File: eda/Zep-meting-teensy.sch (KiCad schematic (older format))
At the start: 12 parts, among them P1 CONN_01X03, Q1 BC547, U1 LM358N, U2 TEMT6000_sparkfun, U3 Teensy3.2, U4 BeexyBox_B

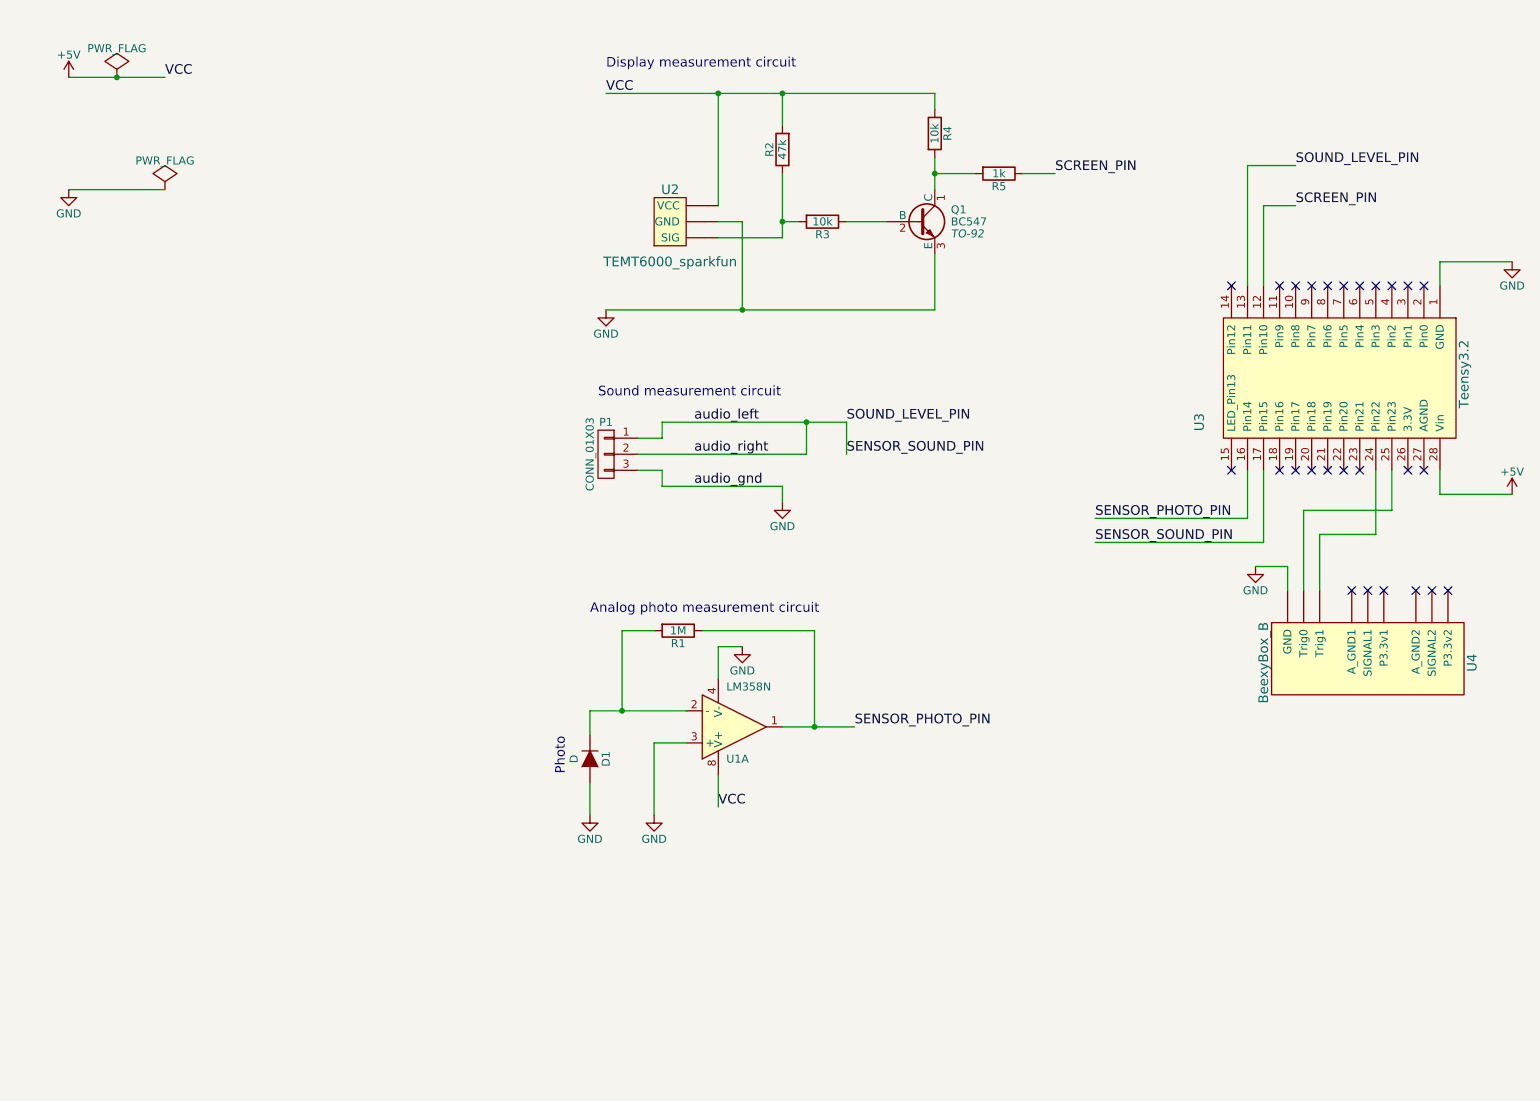
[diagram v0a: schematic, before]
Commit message: Adds opamp display sensor circuit and custom kicad eeschema parts.
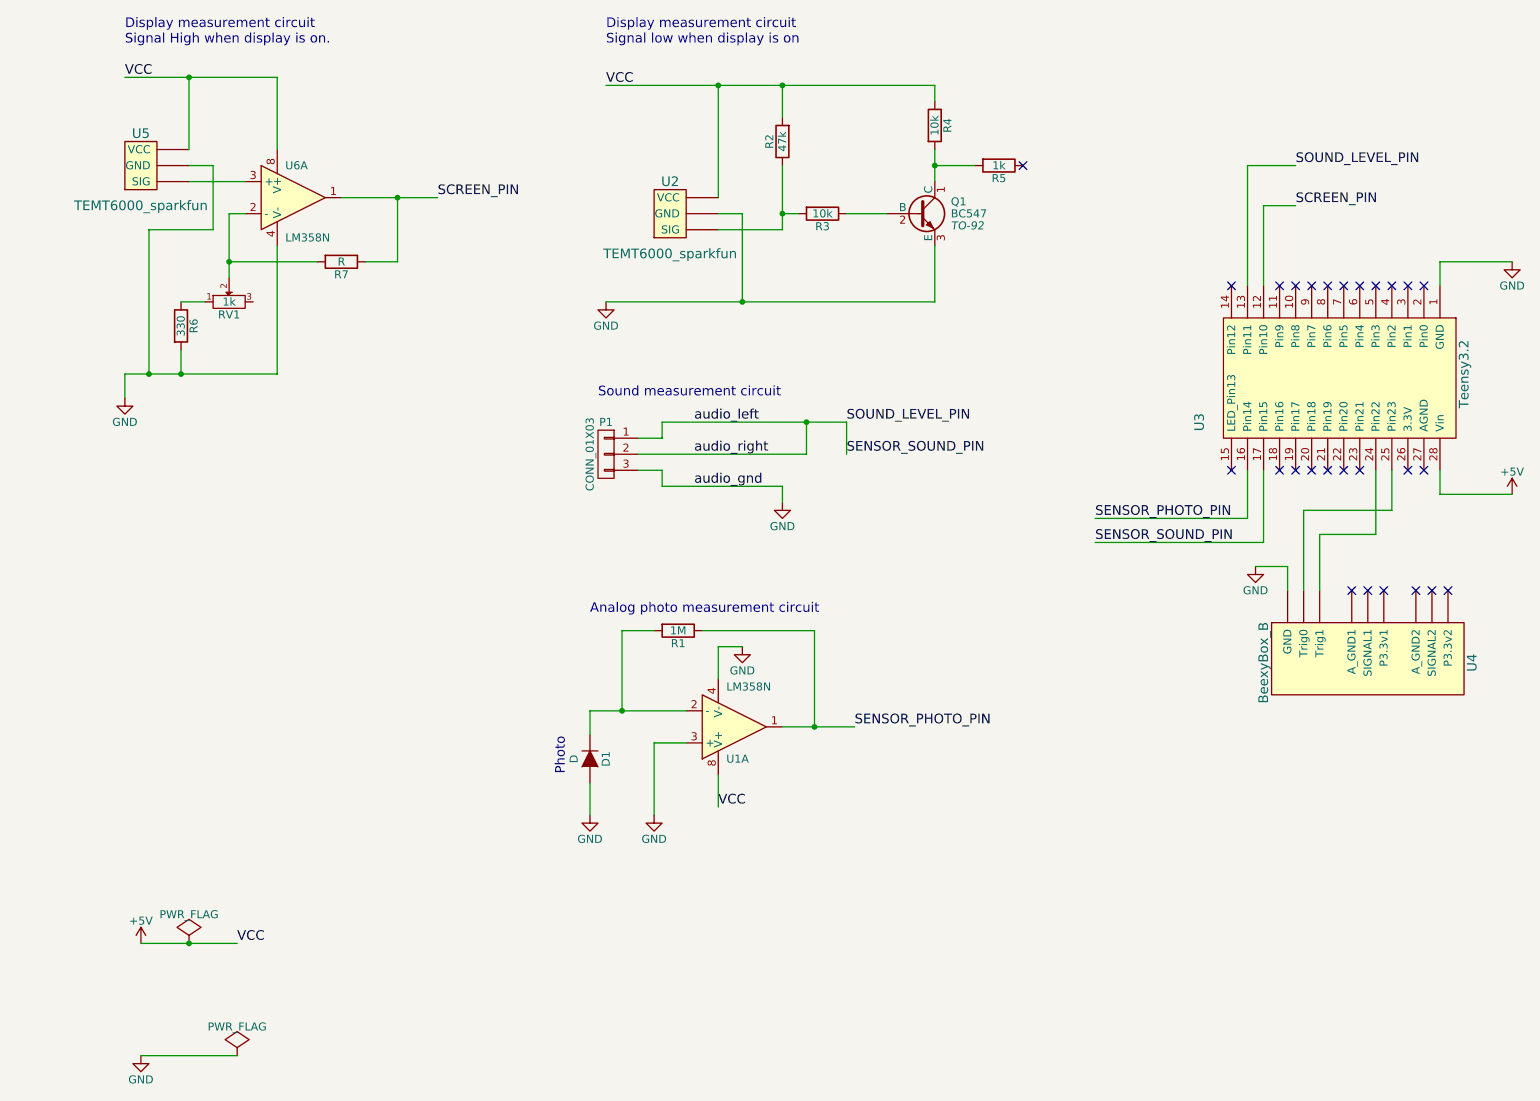
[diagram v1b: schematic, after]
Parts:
- added R6: 330, symbol R
- added R7: R, symbol R
- added RV1: 1k, symbol POT
- added U5: TEMT6000_sparkfun, symbol TEMT6000_sparkfun
- added U6: LM358N, symbol LM358N
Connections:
- net +5V: now also U5.~ (VCC), U6.8 (V+)
- net GND: now also R6.2, U5.~ (VCC), U6.4 (V-)
- net SCREEN_PIN: now also R7.1, U6.1; no longer R5.1
- new net: R6.1, RV1.1
- new net: R7.2, RV1.2, U6.2 (-)
- new net: U5.~ (VCC), U6.3 (+)
- no-connect marks 26 -> 27
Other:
- note added: "Display measurement circuit\nSignal High when display is on."
- note added: "Display measurement circuit\nSignal low when display is on"
- note removed: "Display measurement circuit\n"
- moved on the sheet: Q1, R2, R3, R4, R5, U2

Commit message: Updates electric schema
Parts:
- removed U1: LM358N, symbol LM358N
- added unit 2 of U6
- R7: value R -> 10k
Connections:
- net +5V: now also U6.4 (V-)
- net GND: now also U6.6 (-), U6.8 (V+)
- net SENSOR_PHOTO_PIN: now also U6.7
- net at D1.1 (K), R1.2: now also U6.5 (+)
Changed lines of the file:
@@
-$EndComp
-$Comp
-L LM358N U1
-U 1 1 59317688
-P 5100 5000
-F 0 "U1" H 5050 5200 50  0000 L CNN
-F 1 "LM358N" H 5050 4750 50  0000 L CNN
-F 2 "" H 5100 5000 50  0000 C CNN
-F 3 "" H 5100 5000 50  0000 C CNN
-	1    5100 5000
-	1    0    0    1
 $EndComp
 $Comp
@@
 $EndComp
 $Comp
-L LM358N U6
-U 1 1 594BCA64
-P 2350 1700
-F 0 "U6" H 2300 1900 50  0000 L CNN
-F 1 "LM358N" H 2300 1450 50  0000 L CNN
-F 2 "" H 2350 1700 50  0000 C CNN
-F 3 "" H 2350 1700 50  0000 C CNN
-	1    2350 1700
-	1    0    0    -1
-$EndComp
-$Comp
 L R R7
 U 1 1 594BCB2D
 P 2650 2100
 F 0 "R7" V 2730 2100 50  0000 C CNN
-F 1 "R" V 2650 2100 50  0000 C CNN
+F 1 "10k" V 2650 2100 50  0000 C CNN
 F 2 "" V 2580 2100 50  0000 C CNN
 F 3 "" H 2650 2100 50  0000 C CNN
@@
 Display measurement circuit\nSignal High when display is on.
 NoConn ~ 6900 1500
+$Comp
+L LM358N U6
+U 1 1 594BCA64
+P 2350 1700
+F 0 "U6" H 2300 1900 50  0000 L CNN
+F 1 "LM358N" H 2300 1450 50  0000 L CNN
+F 2 "" H 2350 1700 50  0000 C CNN
+F 3 "" H 2350 1700 50  0000 C CNN
+	1    2350 1700
+	1    0    0    -1
+$EndComp
+$Comp
+L LM358N U6
+U 2 1 594BFA45
+P 5100 5000
+F 0 "U6" H 5050 5200 50  0000 L CNN
+F 1 "LM358N" H 5050 4750 50  0000 L CNN
+F 2 "" H 5100 5000 50  0000 C CNN
+F 3 "" H 5100 5000 50  0000 C CNN
+	2    5100 5000
+	1    0    0    -1
+$EndComp
 $EndSCHEMATC

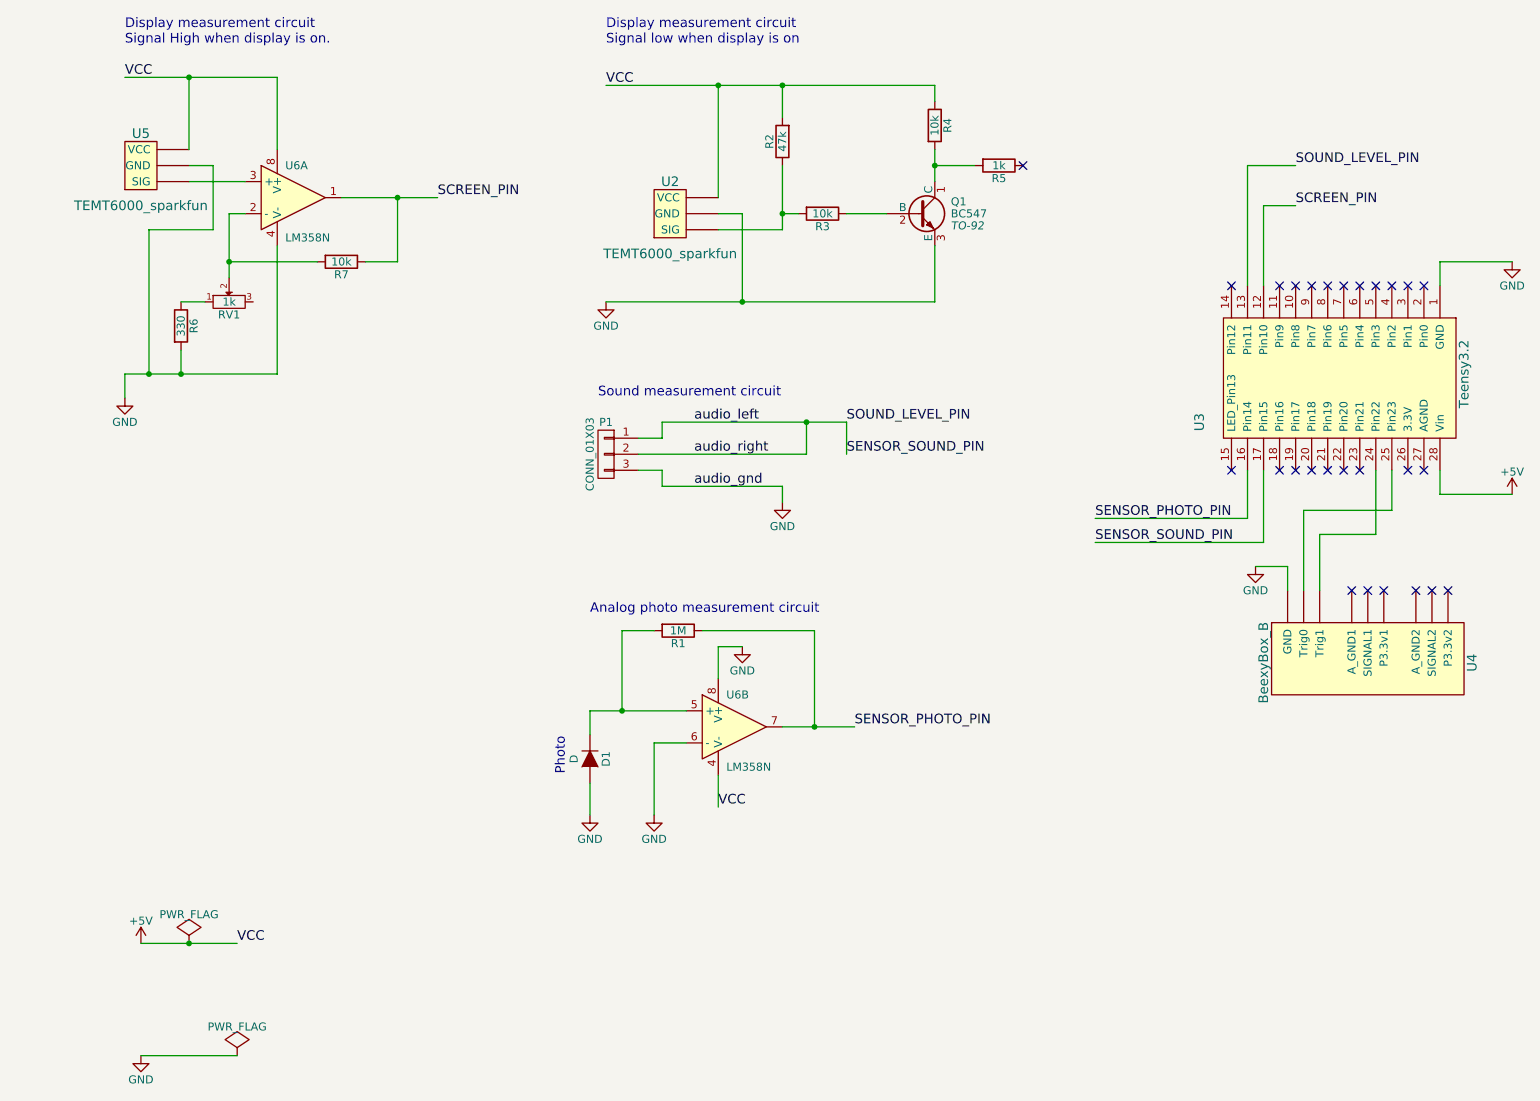
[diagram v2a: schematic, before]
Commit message: Update electric schemes
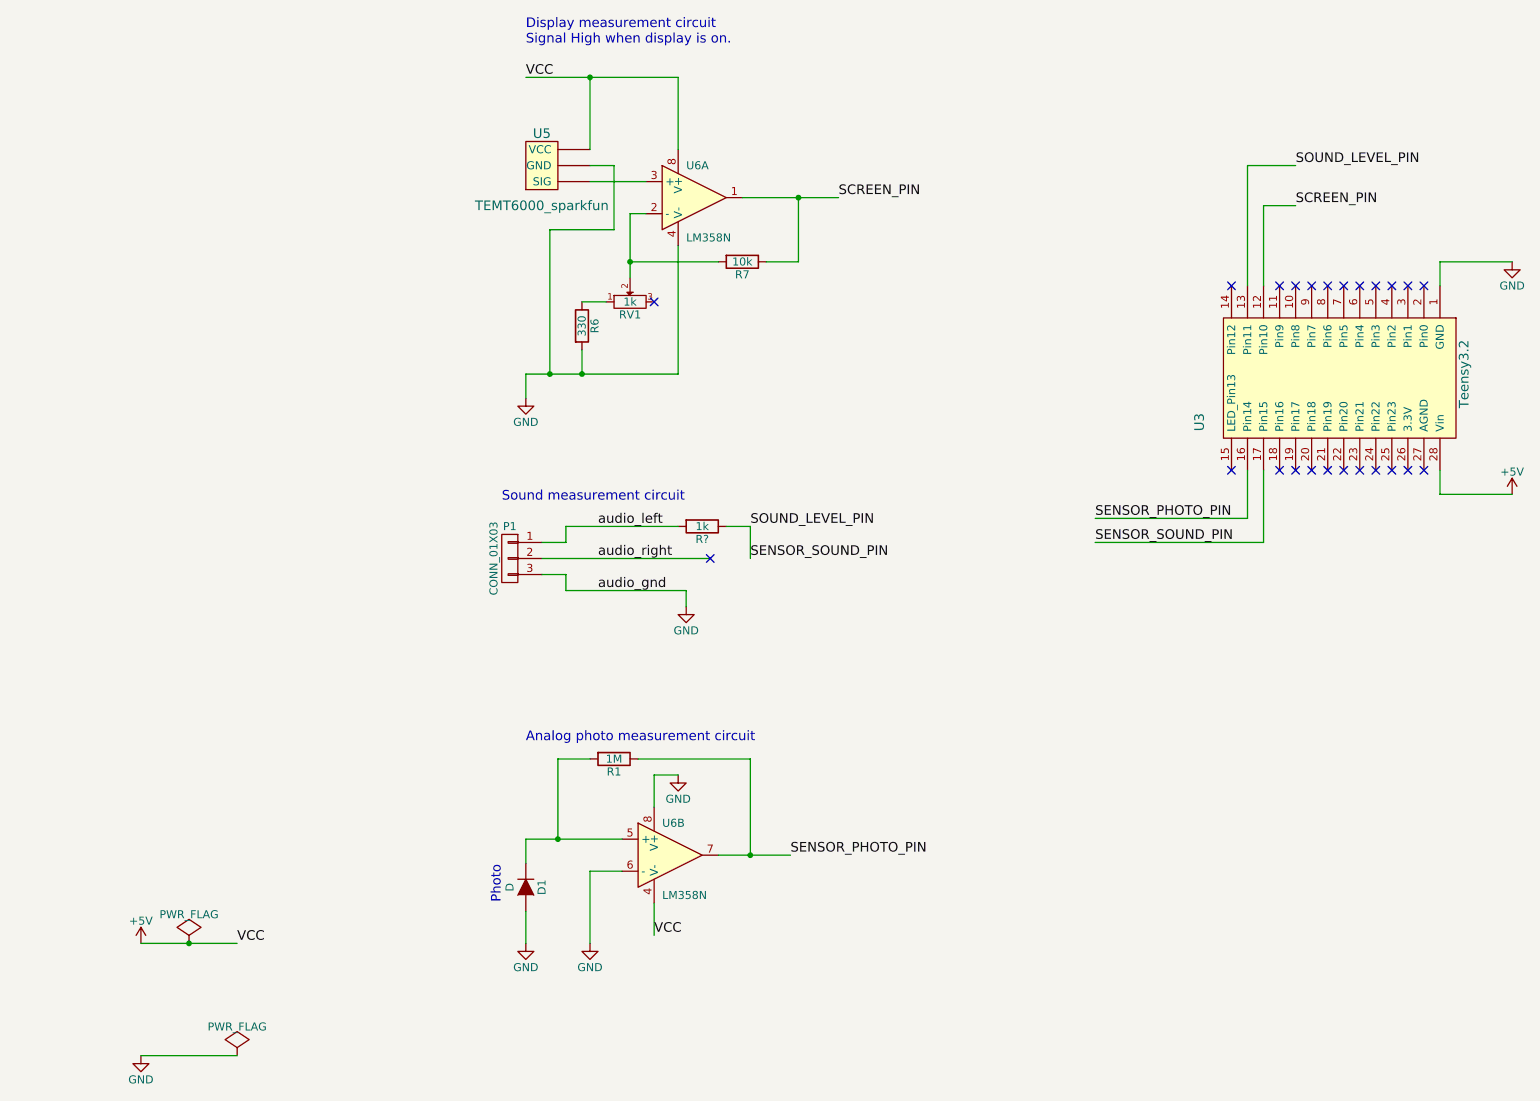
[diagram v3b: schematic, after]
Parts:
- removed Q1: BC547, TO-92, symbol BC547
- removed R2: 47k, symbol R
- removed R3, R4: 10k, symbol R
- removed R5: 1k, symbol R
- removed U2: TEMT6000_sparkfun, symbol TEMT6000_sparkfun
- removed U4: BeexyBox_B, symbol BeexyBox_B
- added R?: 1k, symbol R
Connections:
- net SENSOR_SOUND_PIN: now also R?.1; no longer P1.1 (P1), P1.2 (P2)
- new net audio_left: P1.1 (P1), R?.2
- new net audio_right: P1.2 (P2)
- no-connect marks 27 -> 24
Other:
- note removed: "Display measurement circuit\nSignal low when display is on"
- moved on the sheet: D1, P1, R1, R6, R7, RV1, U5, U6A, U6B
